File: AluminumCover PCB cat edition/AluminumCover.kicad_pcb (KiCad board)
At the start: 2 copper layers, 146 x 76 mm, 8 parts, among them P1 RoundConnectorPad, P2 RoundConnectorPad, P3 RoundConnectorPad, P4 RoundConnectorPad, P5 RoundConnectorPad, P6 RoundConnectorPad, P7 RoundConnectorPad, P8 RoundConnectorPad

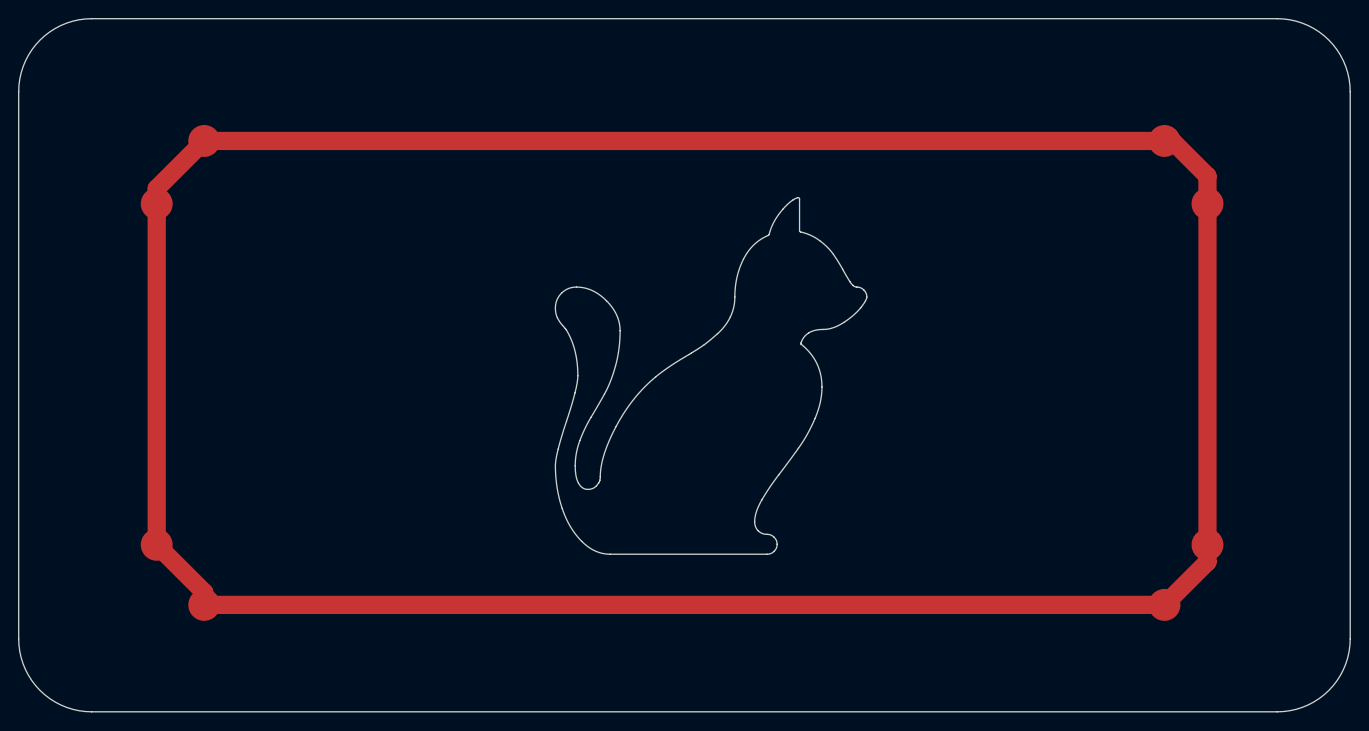
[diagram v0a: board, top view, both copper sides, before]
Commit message: made improvements and started creating usb-c only version
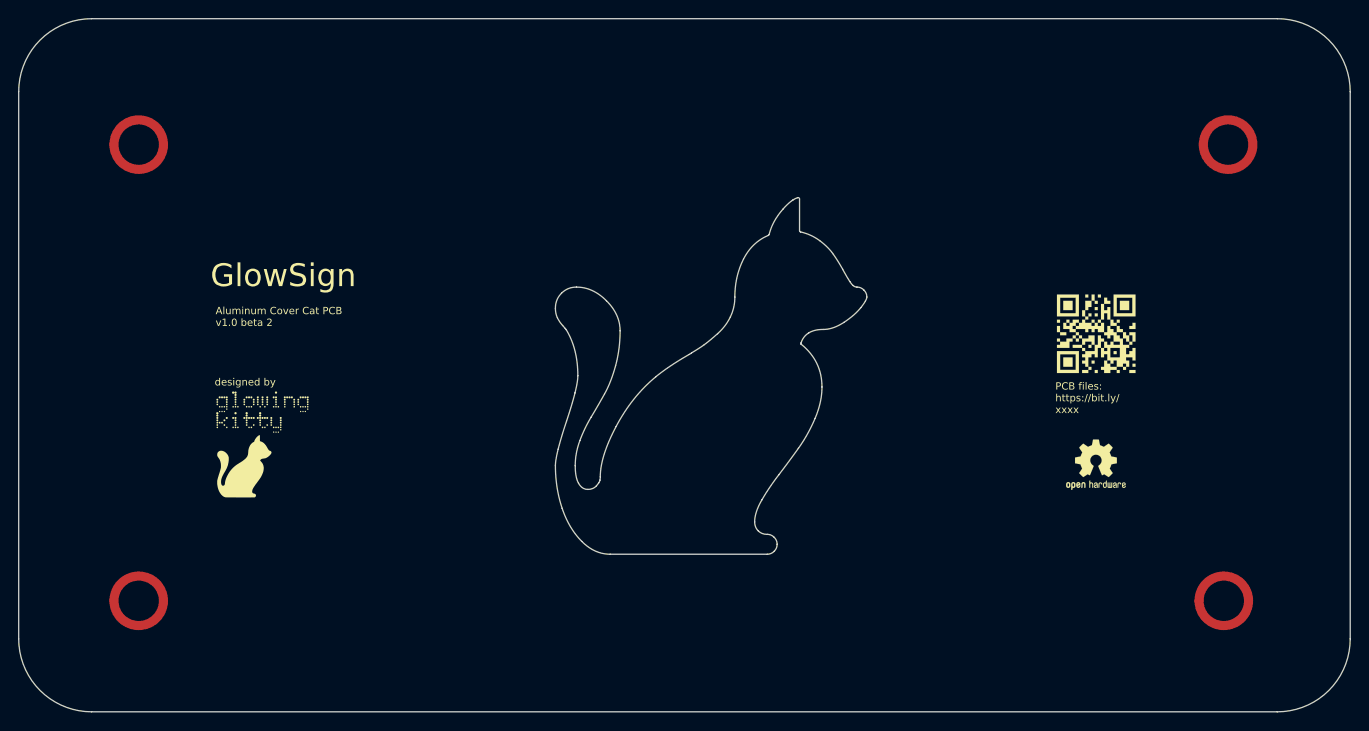
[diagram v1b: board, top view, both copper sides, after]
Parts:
- removed P1, P2, P3, P4, P5, P6, P7, P8: RoundConnectorPad, footprint:RoundSolderPad
- added OSHW logo: OSHW-Logo2_7.3x6mm_SilkScreen, Symbol:OSHW-Logo2_7.3x6mm_SilkScreen, F.Cu at (194.7, 107.0)
- added U1: SMTSO3015CTJ, footprint:SMTSO3030CTJ, F.Cu at (89.7, 71.9)
- added U2: SMTSO3015CTJ, footprint:SMTSO3030CTJ, F.Cu at (89.7, 121.9)
- added U3: SMTSO3015CTJ, footprint:SMTSO3030CTJ, F.Cu at (209.1, 71.9)
- added U4: SMTSO3015CTJ, footprint:SMTSO3030CTJ, F.Cu at (208.7, 121.9)
- added logo: LOGO, LOGO, F.Cu at (103.2, 103.8)
- added qrcode: LOGO, LOGO, F.Cu at (194.7, 92.6)
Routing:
- net GND: track 321.0 -> 0.00 mm
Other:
- board text added: "Aluminum Cover Cat PCB v1.0 beta 2"
- board text added: "GlowSign"
- board text added: "PCB files: https://bit.ly/ xxxx"
- board text added: "designed by"
